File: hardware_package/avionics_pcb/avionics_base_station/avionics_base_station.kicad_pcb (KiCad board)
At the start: 2 copper layers, 2 parts, among them U1 NODEMCU, U2 RFM98

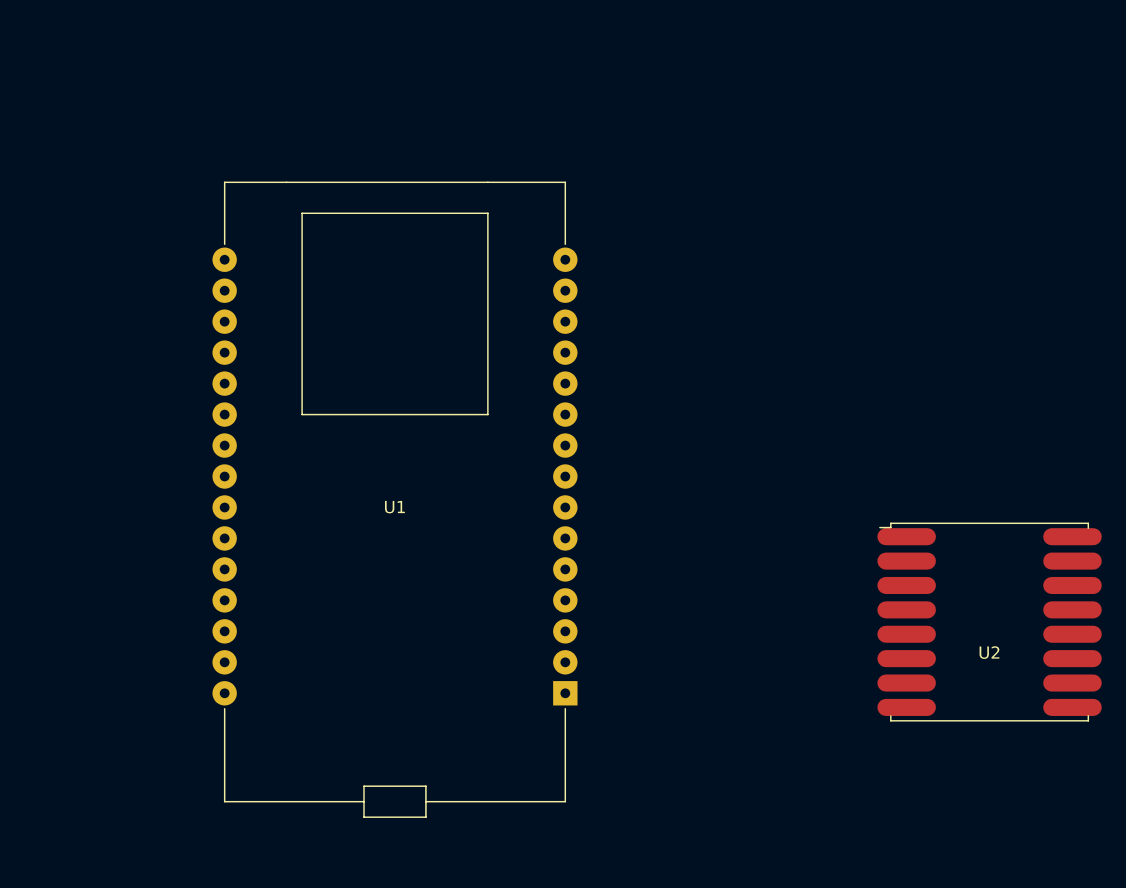
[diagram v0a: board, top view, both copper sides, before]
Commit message: Completed the base station PCB
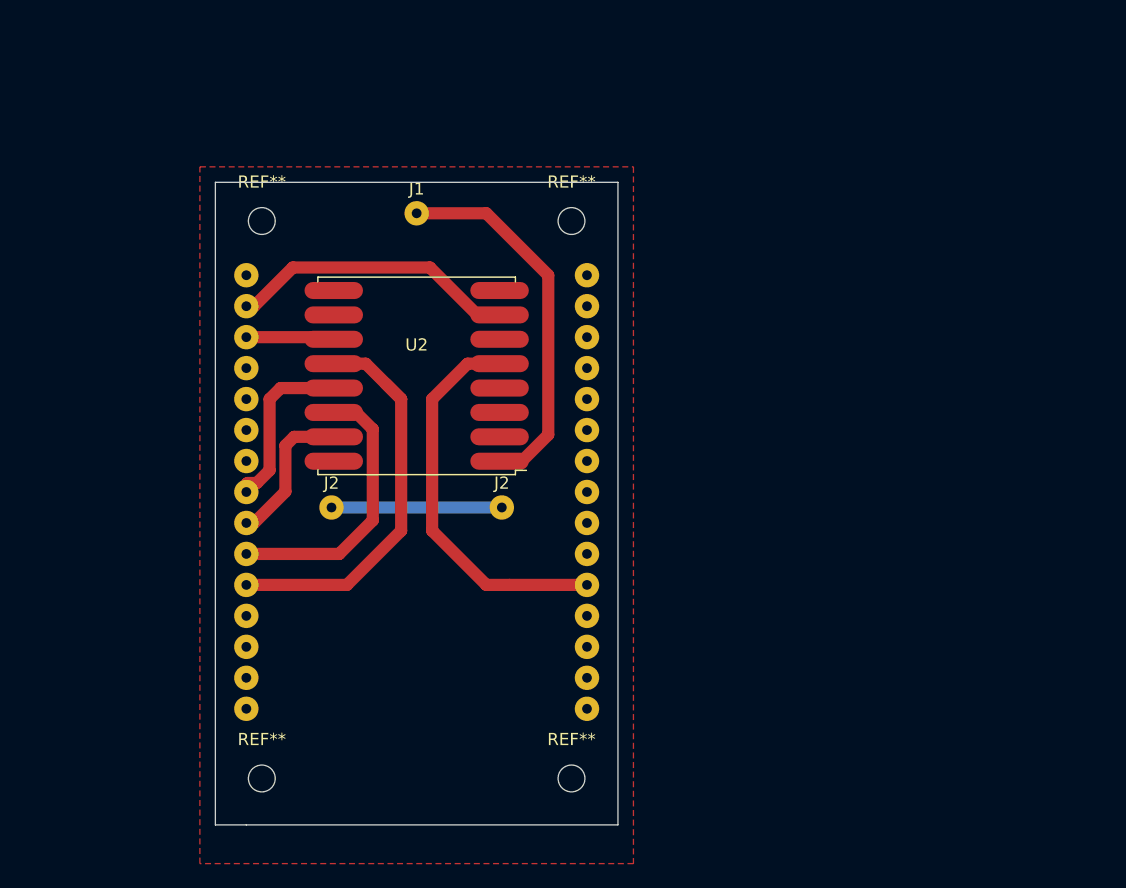
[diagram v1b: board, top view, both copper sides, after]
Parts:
- added J1: ANT, Connector_Wire:SolderWire-0.1sqmm_1x01_D0.4mm_OD1mm, F.Cu at (54.6, 38.1)
- added J2: GND_PASS, Connector_Wire:SolderWire-0.1sqmm_1x01_D0.4mm_OD1mm, F.Cu at (61.6, 62.2)
- added J2: GND_PASS, Connector_Wire:SolderWire-0.1sqmm_1x01_D0.4mm_OD1mm, F.Cu at (47.6, 62.2)
- added REF**: MountingHole_2.2mm_M2, MountingHole:MountingHole_2.2mm_M2, F.Cu at (67.3, 38.7)
- added REF**: MountingHole_2.2mm_M2, MountingHole:MountingHole_2.2mm_M2, F.Cu at (41.9, 38.7)
- added REF**: M2, MountingHole:MountingHole_2.2mm_M2, F.Cu at (67.3, 84.5)
- added REF**: M2, MountingHole:MountingHole_2.2mm_M2, F.Cu at (41.9, 84.5)
- U1: moved to B.Cu
- moved U2 51.1 mm to (54.6, 51.4), turned to 180 degrees
- moved U1 2.18 mm to (54.6, 62.2), turned to 180 degrees
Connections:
- U1 pad 1: /3V3 -> (no net)
- U1 pad 13: (no net) -> Net-(U1-Pad13)
- U1 pad 14: (no net) -> Net-(U1-Pad14)
- U1 pad 17: (no net) -> GND
- U1 pad 2: (no net) -> GND
- U1 pad 20: (no net) -> +3V3
- U1 pad 21: (no net) -> GND
- U1 pad 5: (no net) -> Net-(U1-Pad5)
- U1 pad 6: (no net) -> Net-(U1-Pad6)
- U1 pad 7: (no net) -> Net-(U1-Pad7)
- U1 pad 8: (no net) -> Net-(U1-Pad8)
- U1 pad 9: (no net) -> GND
- U2 pad 1: (no net) -> Net-(J1-Pad1)
- U2 pad 11: (no net) -> Net-(U1-Pad13)
- U2 pad 12: (no net) -> Net-(U1-Pad5)
- U2 pad 13: (no net) -> Net-(U1-Pad8)
- U2 pad 14: (no net) -> Net-(U1-Pad6)
- U2 pad 15: (no net) -> Net-(U1-Pad7)
- U2 pad 16: (no net) -> GND
- U2 pad 2: (no net) -> GND
- U2 pad 5: /3V3 -> +3V3
- U2 pad 7: (no net) -> Net-(U1-Pad14)
- U2 pad 9: (no net) -> GND
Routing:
- net Net-(U1-Pad5): track 0.00 -> 35.1 mm
- net +3V3: track 0.00 -> 33.3 mm
- net Net-(J1-Pad1): track 0.00 -> 29.7 mm
- net Net-(U1-Pad14): track 0.00 -> 24.9 mm
- net Net-(U1-Pad6): track 0.00 -> 24.0 mm
- net GND: track 0.00 -> 14.0 mm
- net Net-(U1-Pad8): track 0.00 -> 13.3 mm
- net Net-(U1-Pad7): track 0.00 -> 11.1 mm
- net Net-(U1-Pad13): track 0.00 -> 6.04 mm
- added copper zone on F.Cu, net GND
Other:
- board outline added: 33 x 52.7 mm
- net class CHAD added: clearance 0.3, trace_width 1, via_dia 2, via_drill 0.8

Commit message: updated the base station PCB
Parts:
- removed the REF** at (67.3, 38.7)
- removed the REF** at (41.9, 38.7)
- removed the REF** at (67.3, 84.5)
- added REF**: MountingHole_2.2mm_M2, MountingHole:MountingHole_2.2mm_M2, F.Cu at (68.6, 38.1)
- added REF**: MountingHole_2.2mm_M2, MountingHole:MountingHole_2.2mm_M2, F.Cu at (40.6, 38.1)
- added REF**: M2, MountingHole:MountingHole_2.2mm_M2, F.Cu at (68.6, 85.7)
- moved J2 18.8 mm to (45.1, 71.1)
- moved J2 4.58 mm to (45.1, 58.4)
- moved REF** 1.80 mm to (40.6, 85.7)
- moved U2 0.63 mm to (55.2, 51.4), turned to 90 degrees
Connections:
- U2 pad 1: Net-(J1-Pad1) -> GND
- U2 pad 10: (no net) -> GND
- U2 pad 11: Net-(U1-Pad13) -> (no net)
- U2 pad 12: Net-(U1-Pad5) -> (no net)
- U2 pad 13: Net-(U1-Pad8) -> +3V3
- U2 pad 14: Net-(U1-Pad6) -> (no net)
- U2 pad 15: Net-(U1-Pad7) -> Net-(U1-Pad14)
- U2 pad 16: GND -> (no net)
- U2 pad 2: GND -> Net-(U1-Pad7)
- U2 pad 3: (no net) -> Net-(U1-Pad6)
- U2 pad 4: (no net) -> Net-(U1-Pad8)
- U2 pad 5: +3V3 -> Net-(U1-Pad5)
- U2 pad 6: (no net) -> Net-(U1-Pad13)
- U2 pad 7: Net-(U1-Pad14) -> (no net)
- U2 pad 8: (no net) -> GND
- U2 pad 9: GND -> Net-(J1-Pad1)
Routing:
- net Net-(J1-Pad1): track 29.7 -> 10.2 mm
- net Net-(U1-Pad13): track 6.04 -> 24.4 mm
- net Net-(U1-Pad5): track 35.1 -> 19.8 mm
- net Net-(U1-Pad14): track 24.9 -> 12.9 mm
- net Net-(U1-Pad6): track 24.0 -> 15.5 mm
- net Net-(U1-Pad8): track 13.3 -> 21.1 mm
- net +3V3: track 33.3 -> 31.9 mm
- net GND: track 14.0 -> 12.7 mm
- net Net-(U1-Pad7): track 11.1 -> 12.1 mm
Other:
- outline, holes or cut-outs redrawn

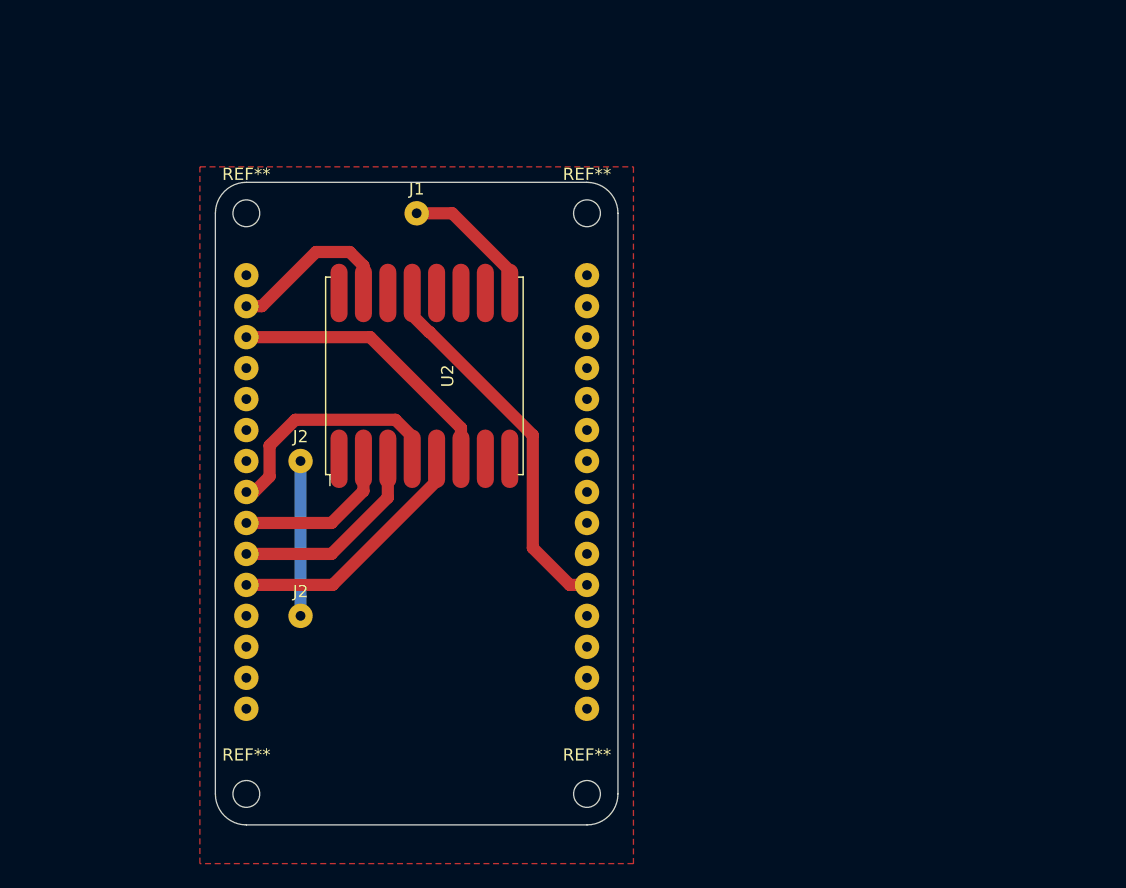
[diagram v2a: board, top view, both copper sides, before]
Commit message: Refactored the PCB and schematic to be placed in a readme. Also created a readme for the Base Station PCB, and added the images
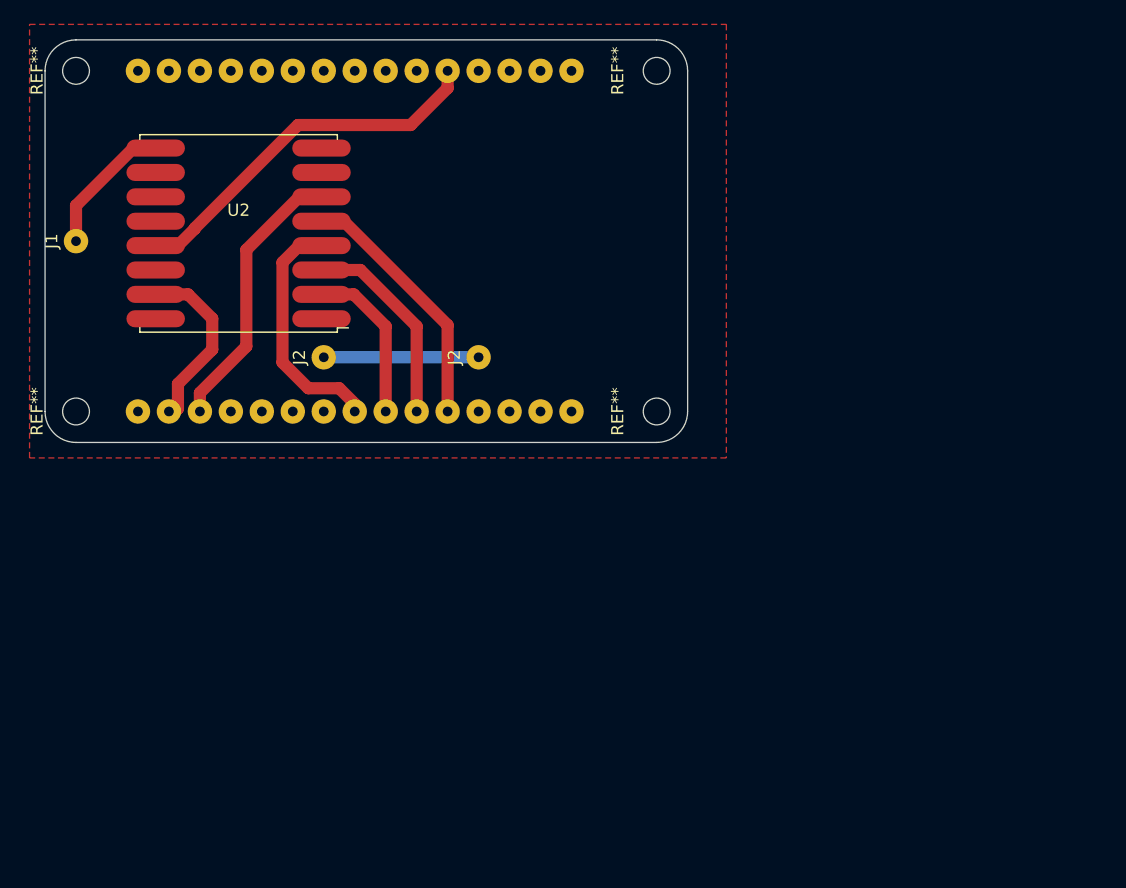
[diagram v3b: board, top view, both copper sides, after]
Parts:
- removed the REF** at (68.6, 38.1)
- removed the REF** at (40.6, 38.1)
- removed the REF** at (68.6, 85.7)
- added REF**: MountingHole_2.2mm_M2, MountingHole:MountingHole_2.2mm_M2, F.Cu at (26.7, 26.4)
- added REF**: MountingHole_2.2mm_M2, MountingHole:MountingHole_2.2mm_M2, F.Cu at (26.7, 54.4)
- added REF**: M2, MountingHole:MountingHole_2.2mm_M2, F.Cu at (74.3, 26.4)
- moved REF** 46.0 mm to (74.3, 54.4), turned to 90 degrees
- moved J1 28.0 mm to (26.7, 40.4), turned to 90 degrees
- moved J2 25.8 mm to (59.7, 49.9), turned to 90 degrees
- moved U1 22.2 mm to (50.8, 40.4), turned to 270 degrees
- moved U2 19.2 mm to (40.0, 39.8), turned to 180 degrees
- moved J2 8.72 mm to (47.0, 49.9), turned to 90 degrees
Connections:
- net Net-(U1-Pad13) renamed RESET
- net Net-(U1-Pad14) renamed INT
- net Net-(U1-Pad5) renamed NSS
- net Net-(U1-Pad6) renamed MOSI
- net Net-(U1-Pad7) renamed MISO
- net Net-(U1-Pad8) renamed SCK
- U1 pad 1: (no net) -> Net-(U1-Pad1)
- U1 pad 10: (no net) -> Net-(U1-Pad10)
- U1 pad 11: (no net) -> Net-(U1-Pad11)
- U1 pad 12: (no net) -> Net-(U1-Pad12)
- U1 pad 15: (no net) -> Net-(U1-Pad15)
- U1 pad 16: (no net) -> Net-(U1-Pad16)
- U1 pad 18: (no net) -> Net-(U1-Pad18)
- U1 pad 19: (no net) -> Net-(U1-Pad19)
- U1 pad 22: (no net) -> Net-(U1-Pad22)
- U1 pad 23: (no net) -> Net-(U1-Pad23)
- U1 pad 24: (no net) -> Net-(U1-Pad24)
- U1 pad 25: (no net) -> Net-(U1-Pad25)
- U1 pad 26: (no net) -> Net-(U1-Pad26)
- U1 pad 27: (no net) -> Net-(U1-Pad27)
- U1 pad 28: (no net) -> Net-(U1-Pad28)
- U1 pad 29: (no net) -> Net-(U1-Pad29)
- U1 pad 3: (no net) -> Net-(U1-Pad3)
- U1 pad 30: (no net) -> Net-(U1-Pad30)
- U1 pad 4: (no net) -> Net-(U1-Pad4)
- U2 pad 11: (no net) -> Net-(U2-Pad11)
- U2 pad 12: (no net) -> Net-(U2-Pad12)
- U2 pad 14: (no net) -> Net-(U2-Pad14)
- U2 pad 16: (no net) -> Net-(U2-Pad16)
- U2 pad 7: (no net) -> Net-(U2-Pad7)
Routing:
- net INT: track 12.9 -> 16.1 mm
- net GND: track 12.7 -> 15.2 mm
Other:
- board size 33 x 52.7 mm -> 52.7 x 33 mm
